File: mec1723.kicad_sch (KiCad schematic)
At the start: 82 parts, among them J3001 PinHeader_2x5_P1.27mm_SMD, J3002 PinHeader_2x5_P1.27mm_SMD, J3003 PinHeader_2x5_P1.27mm_SMD, J3004 PinHeader_2x5_P1.27mm_SMD, J3005 PinHeader_2x5_P1.27mm_SMD, J3006 PinHeader_2x5_P1.27mm_SMD, J3007 PinHeader_2x5_P1.27mm_SMD, J3008 PinHeader_2x5_P1.27mm_SMD, J3009 PinHeader_2x5_P1.27mm_SMD, J3010 PinHeader_2x5_P1.27mm_SMD, J3011 PinHeader_2x5_P1.27mm_SMD, SW3001 SW_B3U-1000P_SMD, SW3002 SW_B3U-1000P_SMD, SW3003 SW_B3U-1000P_SMD, U3001 MEC1723N-B0-I/SZ, Y3001 Resonator_32.768kHz_ECX-31B

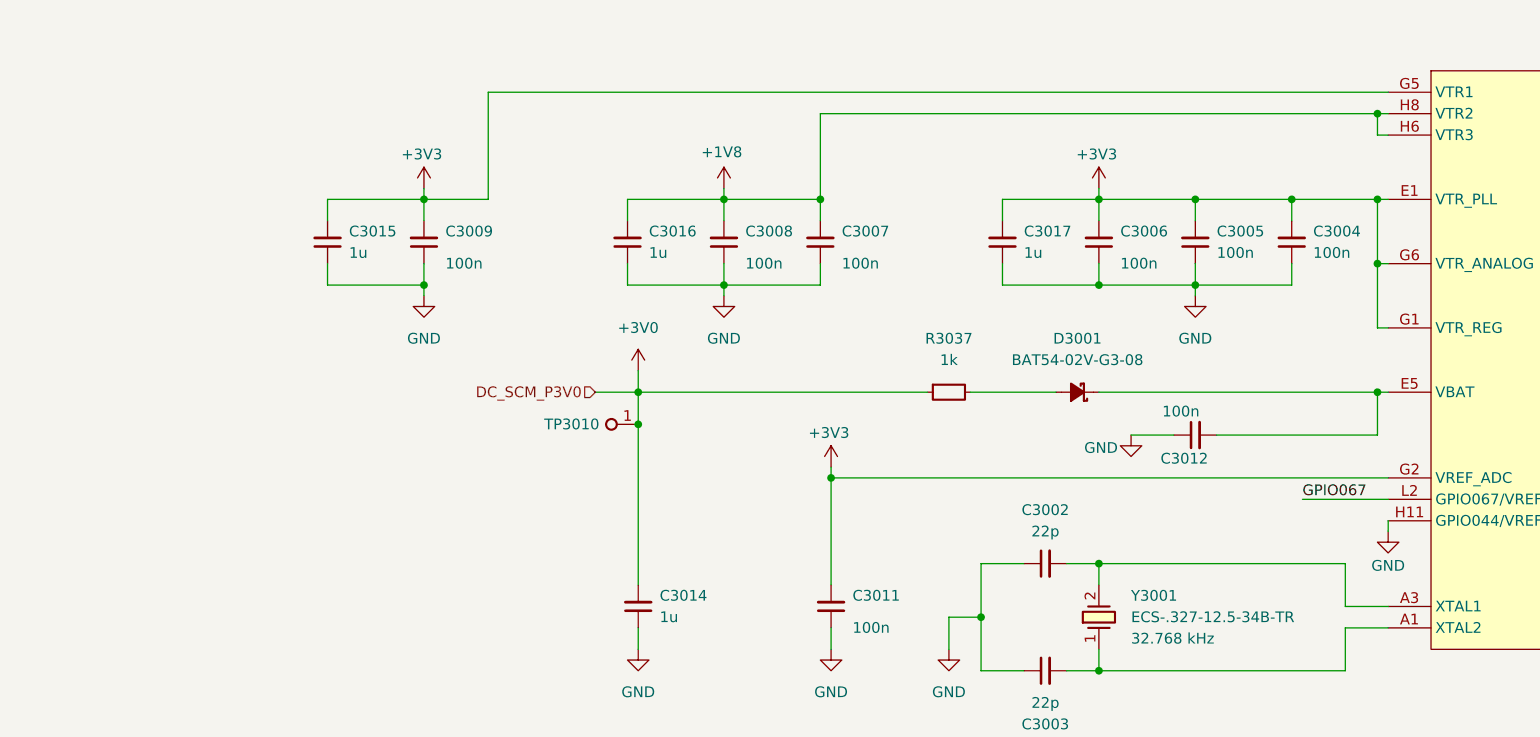
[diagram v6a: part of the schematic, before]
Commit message: [#103696] Add 0 ohm resistors to power rails  on the scheatic, changed C7001 from 10uF to 1uF
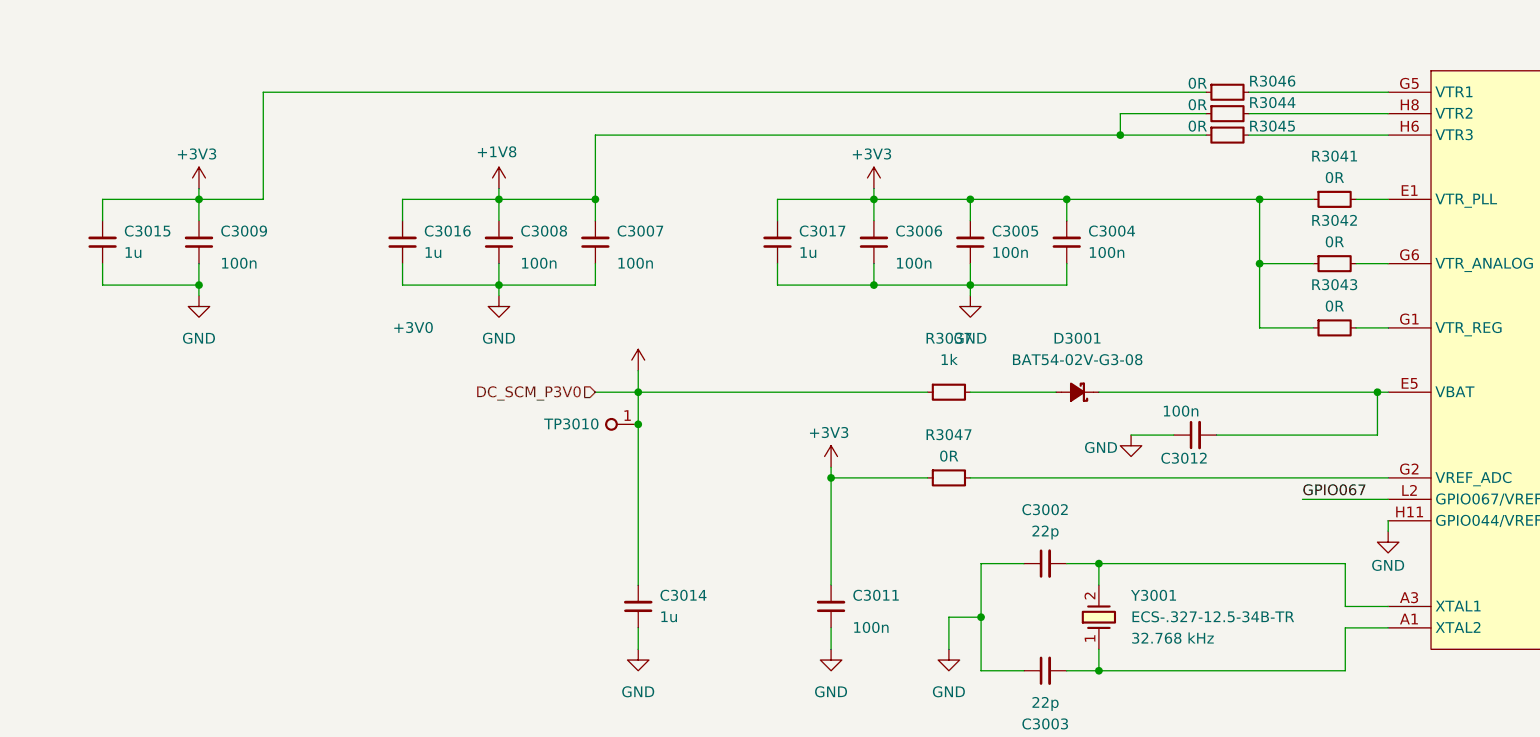
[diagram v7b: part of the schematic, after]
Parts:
- added R3041, R3042, R3043, R3044, R3045, R3046, R3047: R_0R_0402, antmicro-footprints:R_0402_1005Metric, symbol Antmicro Symbols:R_0R_0402
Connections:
- net +1V8: now also R3044.1, R3045.1; no longer U3001.H6 (VTR3), U3001.H8 (VTR2)
- net +3V3: now also R3041.1, R3042.1, R3043.1, R3046.1, R3047.1; no longer U3001.E1 (VTR_PLL), U3001.G1 (VTR_REG), U3001.G2 (VREF_ADC), U3001.G5 (VTR1), U3001.G6 (VTR_ANALOG)
- new net: R3041.2, U3001.E1 (VTR_PLL)
- new net: R3046.2, U3001.G5 (VTR1)
- new net: R3043.2, U3001.G1 (VTR_REG)
- new net: R3047.2, U3001.G2 (VREF_ADC)
- new net: R3042.2, U3001.G6 (VTR_ANALOG)
- new net: R3045.2, U3001.H6 (VTR3)
- new net: R3044.2, U3001.H8 (VTR2)
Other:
- moved on the sheet: C3004, C3005, C3006, C3007, C3008, C3009, C3015, C3016, C3017

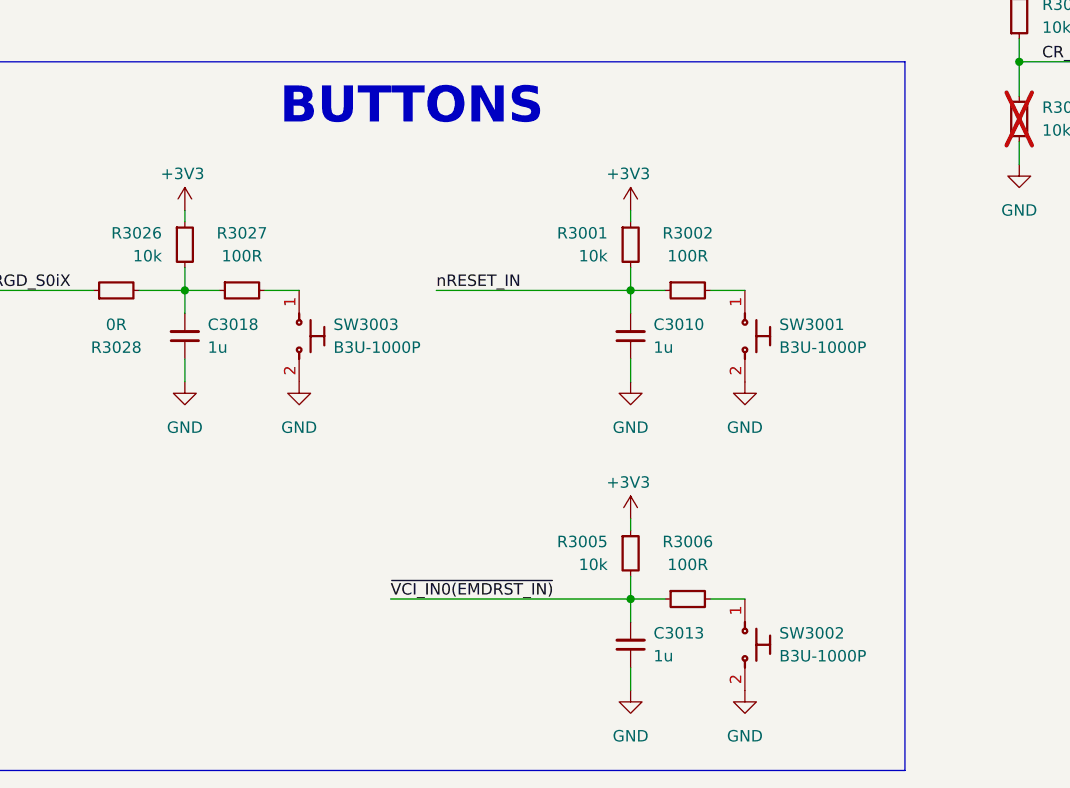
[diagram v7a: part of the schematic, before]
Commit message: [#103697] Change key sectors placement (DC-DC, 7seg, Flash, FTDI), Change buttons, Change DC-SCM connector to angled header
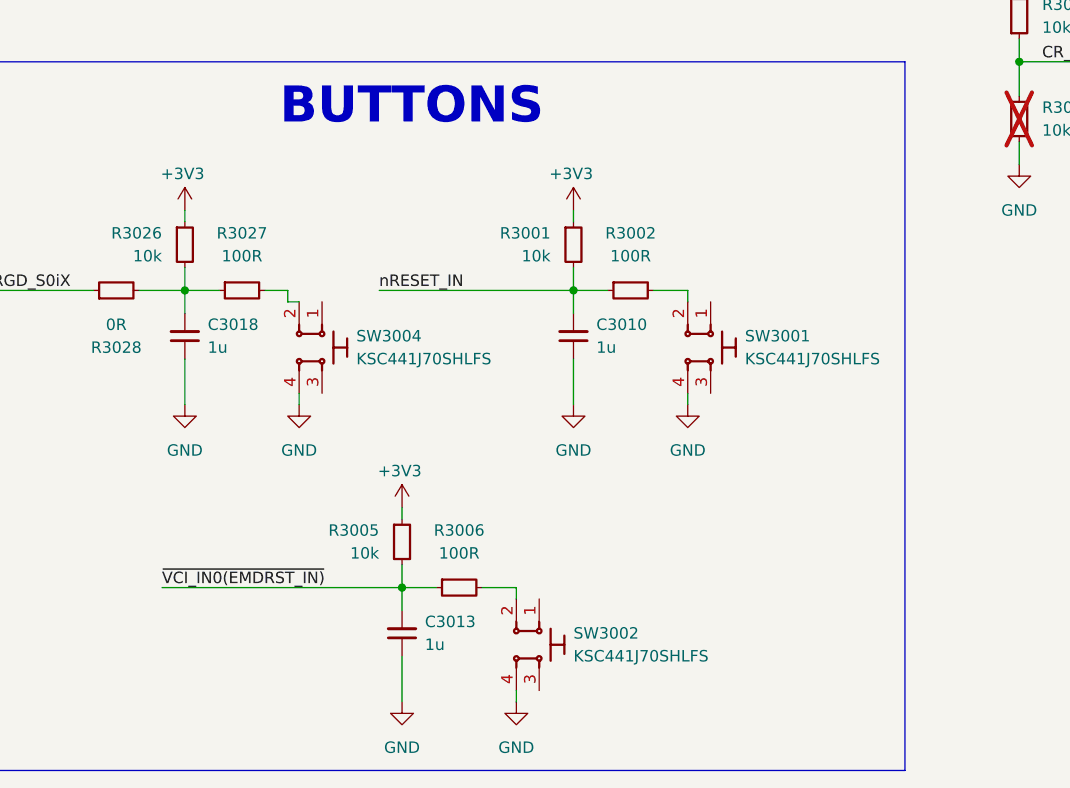
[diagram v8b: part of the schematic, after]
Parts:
- removed SW3001, SW3002, SW3003: SW_B3U-1000P_SMD, antmicro-footprints:SW_B3U-1000P_SMD, symbol Antmicro Symbols:SW_B3U-1000P_SMD
- added SW3001, SW3002, SW3004: SW_KSC441J70SHLFS_SMD, antmicro-footprints:SW_KSC441J70SHLFS_SMD, symbol Antmicro Symbols:SW_KSC441J70SHLFS_SMD
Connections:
- net GND: now also SW3001.4, SW3002.4, SW3004.4
- net at R3027.2: now also SW3004.2
- net at R3006.2: now also SW3002.2
- net at R3002.2: now also SW3001.2
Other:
- moved on the sheet: C3010, C3013, R3001, R3002, R3005, R3006
